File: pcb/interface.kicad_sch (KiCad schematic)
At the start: 46 parts

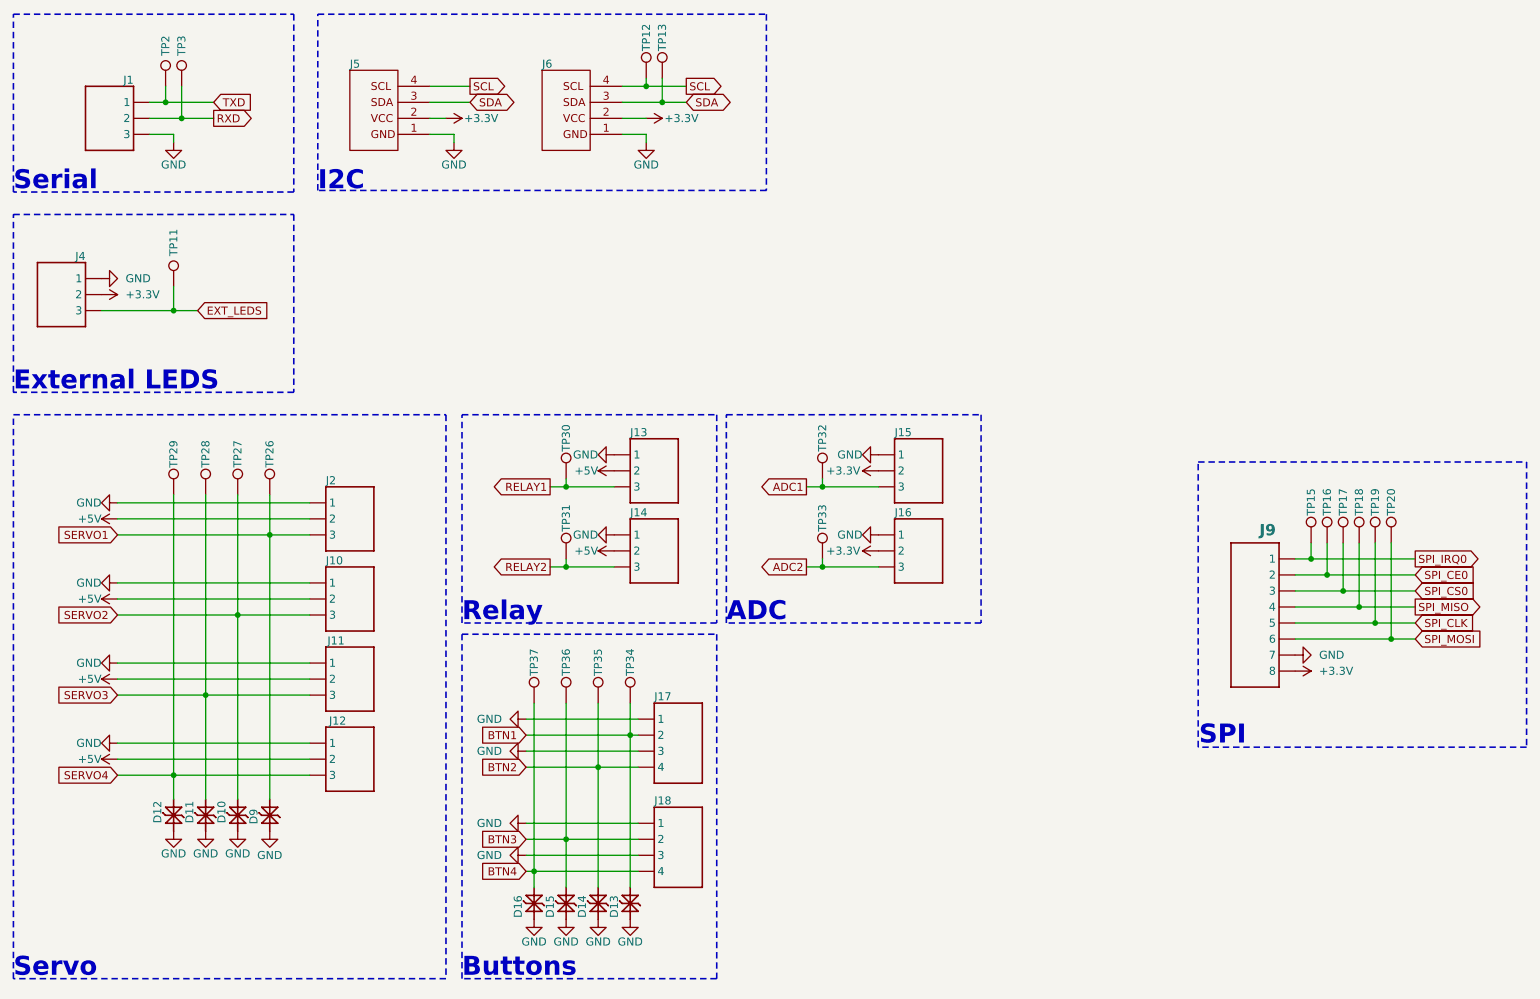
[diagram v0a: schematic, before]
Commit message: Added RF connector; re-placed and re-routed
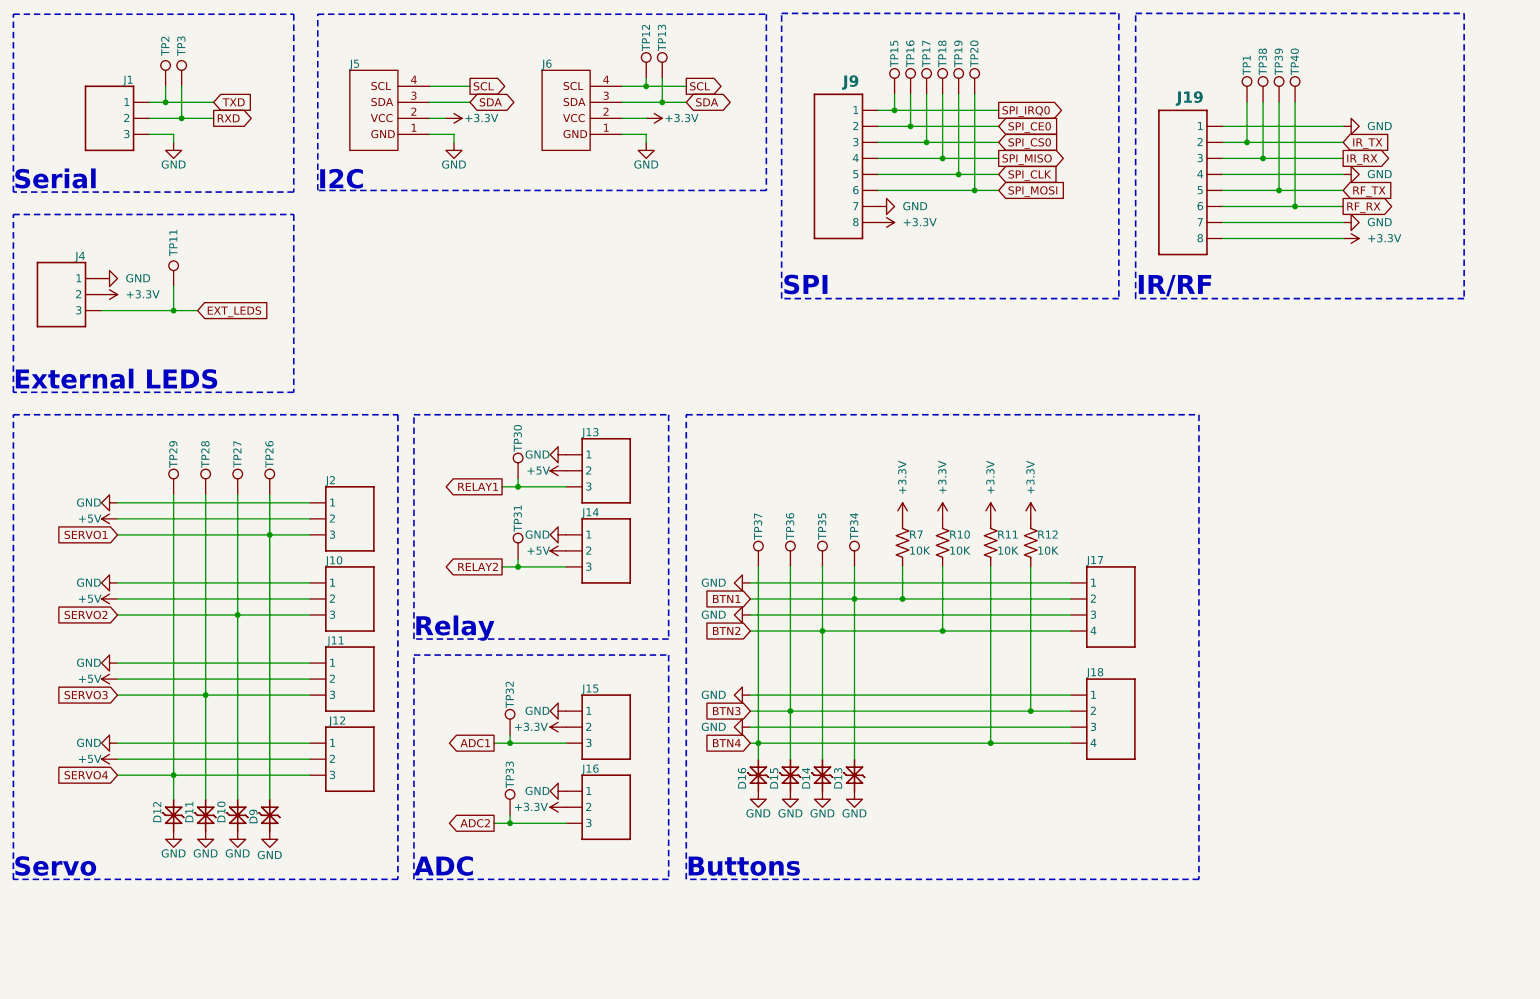
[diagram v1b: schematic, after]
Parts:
- added J19: ~, CRGM Connector:JST_SH_BM08B-SRSS-TB_1x08-1MP_P1.00mm_Vertical, symbol CRGM Connector:JST-SH-8
- added R10, R11, R12, R7: 10K, CRGM Passive:R_0603_1608Metric, symbol Device:R_US
- added TP1, TP38, TP39, TP40: ~, CRGM Mechanical:TestPoint_Pad_D1.0mm, symbol Connector:TestPoint
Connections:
- net +3.3V: now also J19.8, R10.1, R11.1, R12.1, R7.1
- net BTN1: now also R7.2
- net BTN2: now also R10.2
- net BTN3: now also R12.2
- net BTN4: now also R11.2
- net GND: now also J19.1, J19.4, J19.7
- new net IR_RX: J19.3, TP38.1
- new net IR_TX: J19.2, TP1.1
- new net RF_RX: J19.6, TP40.1
- new net RF_TX: J19.5, TP39.1
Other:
- note added: "IR/RF"
- title: Client -> Aquarius Client
- moved on the sheet: D13, D14, D15, D16, J13, J14, J15, J16, J17, J18, J9, TP15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

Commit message: Removed indictors sheet
Fixed attribute consistency with schematic and symbols
Moved logos to separate box
Updated DRC warnings/ignore
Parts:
- J1, J10, J11, J12, J13, J14, J15, J16, J2, J4: Digikey (none) -> 455-BM04B-SRSS-TBTR-ND
- J17, J18: LCSC C2919601 -> C2763614

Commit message: Updated part attributes for consistency
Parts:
- R10, R11, R12, R7: Tolerance (none) -> 5%
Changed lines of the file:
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@@
 			)
 		)
-		(property "Datasheet" "~"
+		(property "Datasheet" "https://bourns.com/docs/product-datasheets/cr.pdf?sfvrsn=574d41f6_14"
 			(at 176.53 99.06 0)
 			(effects
@@
 			)
 		)
+		(property "Tolerance" "5%"
+			(at 176.53 99.06 0)
+			(effects
+				(font
+					(size 1.27 1.27)
+				)
+				(hide yes)
+			)
+		)
 		(pin "2"
 		)
@@
 			)
 		)
-		(property "Datasheet" "~"
+		(property "Datasheet" "https://bourns.com/docs/product-datasheets/cr.pdf?sfvrsn=574d41f6_14"
 			(at 170.18 99.06 0)
 			(effects
@@
 			)
 		)
+		(property "Tolerance" "5%"
+			(at 170.18 99.06 0)
+			(effects
+				(font
+					(size 1.27 1.27)
+				)
+				(hide yes)
+			)
+		)
 		(pin "2"
 		)
@@
 			)
 		)
-		(property "Datasheet" ""
+		(property "Datasheet" "https://www.jst-mfg.com/product/pdf/eng/eSH.pdf"
 			(at 99.06 24.13 0)
 			(effects
@@
 			)
 		)
-		(property "Description" "I2C Qwiic Connector 1mm pitch JST"
+		(property "Description" "4 Position, 1mm pitch"
 			(at 103.378 38.1 0)
 			(effects
@@
 			)
 		)
-		(property "Datasheet" ""
+		(property "Datasheet" "https://www.jst-mfg.com/product/pdf/eng/eSH.pdf"
 			(at 68.58 24.13 0)
 			(effects
@@
 			)
 		)
-		(property "Description" "I2C Qwiic Connector 1mm pitch JST"
+		(property "Description" "4 Position, 1mm pitch"
 			(at 72.898 38.1 0)
 			(effects
@@
 			)
 		)
-		(property "Datasheet" "~"
+		(property "Datasheet" "https://bourns.com/docs/product-datasheets/cr.pdf?sfvrsn=574d41f6_14"
 			(at 156.21 99.06 0)
 			(effects
@@
 			)
 		)
+		(property "Tolerance" "5%"
+			(at 156.21 99.06 0)
+			(effects
+				(font
+					(size 1.27 1.27)
+				)
+				(hide yes)
+			)
+		)
 		(pin "2"
 		)
@@
 			)
 		)
-		(property "Datasheet" "~"
+		(property "Datasheet" "https://bourns.com/docs/product-datasheets/cr.pdf?sfvrsn=574d41f6_14"
 			(at 162.56 99.06 0)
 			(effects
@@
 			(at 162.56 99.06 0)
 			(effects
+				(font
+					(size 1.27 1.27)
+				)
+				(hide yes)
+			)
+		)
+		(property "Tolerance" "5%"
+			(at 162.56 99.06 0)
+			(effects

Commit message: fixed LCSC part numbers
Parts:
- J1, J10, J11, J12, J13, J14, J15, J16, J2, J4: Digikey 455-BM04B-SRSS-TBTR-ND -> 455-BM03B-SRSS-TBTR-ND; LCSC C2919601 -> C2904985; MPN BM04B-SRSS-TB -> BM03B-SRSS-TB; Mouser 306-BM04BSRSSTBTLFSN -> 306-BM03BSRSSTBTLFSN
- J17, J18: LCSC C2763614 -> C2904986
- J5, J6: LCSC C2919601 -> C2904986
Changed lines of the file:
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@@
 			)
 		)
-		(property "LCSC" "C2919601"
+		(property "LCSC" "C2904985"
 			(at 105.41 154.94 0)
 			(effects
@@
 			)
 		)
-		(property "MPN" "BM04B-SRSS-TB"
+		(property "MPN" "BM03B-SRSS-TB"
 			(at 105.41 152.908 0)
 			(effects
@@
 			)
 		)
-		(property "Mouser" "306-BM04BSRSSTBTLFSN"
+		(property "Mouser" "306-BM03BSRSSTBTLFSN"
 			(at 105.41 159.766 0)
 			(effects
@@
 			)
 		)
-		(property "Digikey" "455-BM04B-SRSS-TBTR-ND"
+		(property "Digikey" "455-BM03B-SRSS-TBTR-ND"
 			(at 105.41 157.226 0)
 			(effects
@@
 			)
 		)
-		(property "LCSC" "C2919601"
+		(property "LCSC" "C2904985"
 			(at 64.77 147.32 0)
 			(effects
@@
 			)
 		)
-		(property "MPN" "BM04B-SRSS-TB"
+		(property "MPN" "BM03B-SRSS-TB"
 			(at 64.77 145.288 0)
 			(effects
@@
 			)
 		)
-		(property "Mouser" "306-BM04BSRSSTBTLFSN"
+		(property "Mouser" "306-BM03BSRSSTBTLFSN"
 			(at 64.77 152.146 0)
 			(effects
@@
 			)
 		)
-		(property "Digikey" "455-BM04B-SRSS-TBTR-ND"
+		(property "Digikey" "455-BM03B-SRSS-TBTR-ND"
 			(at 64.77 149.606 0)
 			(effects
@@
 			)
 		)
-		(property "LCSC" "C2919601"
+		(property "LCSC" "C2904985"
 			(at 64.77 134.62 0)
 			(effects
@@
 			)
 		)
-		(property "MPN" "BM04B-SRSS-TB"
+		(property "MPN" "BM03B-SRSS-TB"
 			(at 64.77 132.588 0)
 			(effects
@@
 			)
 		)
-		(property "Mouser" "306-BM04BSRSSTBTLFSN"
+		(property "Mouser" "306-BM03BSRSSTBTLFSN"
 			(at 64.77 139.446 0)
 			(effects
@@
 			)
 		)
-		(property "Digikey" "455-BM04B-SRSS-TBTR-ND"
+		(property "Digikey" "455-BM03B-SRSS-TBTR-ND"
 			(at 64.77 136.906 0)
 			(effects
@@
 			)
 		)
-		(property "LCSC" "C2919601"
+		(property "LCSC" "C2904985"
 			(at 26.67 73.66 0)
 			(effects
@@
 			)
 		)
-		(property "MPN" "BM04B-SRSS-TB"
+		(property "MPN" "BM03B-SRSS-TB"
 			(at 26.67 71.628 0)
 			(effects
@@
 			)
 		)
-		(property "Mouser" "306-BM04BSRSSTBTLFSN"
+		(property "Mouser" "306-BM03BSRSSTBTLFSN"
 			(at 26.67 78.486 0)
 			(effects
@@
 			)
 		)
-		(property "Digikey" "455-BM04B-SRSS-TBTR-ND"
+		(property "Digikey" "455-BM03B-SRSS-TBTR-ND"
 			(at 26.67 75.946 0)
 			(effects
@@
 			)
 		)
-		(property "LCSC" "C2919601"
+		(property "LCSC" "C2904985"
 			(at 64.77 109.22 0)
 			(effects
@@
 			)
 		)
-		(property "MPN" "BM04B-SRSS-TB"
+		(property "MPN" "BM03B-SRSS-TB"
 			(at 64.77 107.188 0)
 			(effects
@@
 			)
 		)
-		(property "Mouser" "306-BM04BSRSSTBTLFSN"
+		(property "Mouser" "306-BM03BSRSSTBTLFSN"
 			(at 64.77 114.046 0)
 			(effects
@@
 			)
 		)
-		(property "Digikey" "455-BM04B-SRSS-TBTR-ND"
+		(property "Digikey" "455-BM03B-SRSS-TBTR-ND"
 			(at 64.77 111.506 0)
 			(effects
@@
 			)
 		)
-		(property "LCSC" "C2919601"
+		(property "LCSC" "C2904985"
 			(at 64.77 121.92 0)
 			(effects
@@
 			)
 		)
-		(property "MPN" "BM04B-SRSS-TB"
+		(property "MPN" "BM03B-SRSS-TB"
 			(at 64.77 119.888 0)
 			(effects
@@
 			)
 		)
-		(property "Mouser" "306-BM04BSRSSTBTLFSN"
+		(property "Mouser" "306-BM03BSRSSTBTLFSN"
 			(at 64.77 126.746 0)
 			(effects
@@
 			)
 		)
-		(property "Digikey" "455-BM04B-SRSS-TBTR-ND"
+		(property "Digikey" "455-BM03B-SRSS-TBTR-ND"
 			(at 64.77 124.206 0)
 			(effects
@@
 			)
 		)
-		(property "LCSC" "C2919601"
+		(property "LCSC" "C2904985"
 			(at 105.41 142.24 0)
 			(effects
@@
 			)
 		)
-		(property "MPN" "BM04B-SRSS-TB"
+		(property "MPN" "BM03B-SRSS-TB"
 			(at 105.41 140.208 0)
 			(effects
@@
 			)
 		)
-		(property "Mouser" "306-BM04BSRSSTBTLFSN"
+		(property "Mouser" "306-BM03BSRSSTBTLFSN"
 			(at 105.41 147.066 0)
 			(effects
@@
 			)
 		)
-		(property "Digikey" "455-BM04B-SRSS-TBTR-ND"
+		(property "Digikey" "455-BM03B-SRSS-TBTR-ND"
 			(at 105.41 144.526 0)
 			(effects
@@
 			)
 		)
-		(property "LCSC" "C2919601"
+		(property "LCSC" "C2904986"
 			(at 103.886 50.292 0)
 			(effects
@@
 			)
 		)
-		(property "LCSC" "C2919601"
+		(property "LCSC" "C2904986"
 			(at 73.406 50.292 0)
 			(effects
@@
 			)
 		)
-		(property "LCSC" "C2919601"
+		(property "LCSC" "C2904985"
 			(at 34.29 45.72 0)
 			(effects
@@
 			)
 		)
-		(property "MPN" "BM04B-SRSS-TB"
+		(property "MPN" "BM03B-SRSS-TB"
 			(at 34.29 43.688 0)
 			(effects
@@
 			)
 		)
-		(property "Mouser" "306-BM04BSRSSTBTLFSN"
+		(property "Mouser" "306-BM03BSRSSTBTLFSN"
 			(at 34.29 50.546 0)
 			(effects
@@
 			)
 		)
-		(property "Digikey" "455-BM04B-SRSS-TBTR-ND"
+		(property "Digikey" "455-BM03B-SRSS-TBTR-ND"
 			(at 34.29 48.006 0)
 			(effects
@@
 			)
 		)
-		(property "LCSC" "C2763614"
+		(property "LCSC" "C2904986"
 			(at 188.468 105.41 0)
 			(effects
@@
 			)
 		)
-		(property "LCSC" "C2919601"
+		(property "LCSC" "C2904985"
 			(at 105.41 114.3 0)
 			(effects
@@
 			)
 		)
-		(property "MPN" "BM04B-SRSS-TB"
+		(property "MPN" "BM03B-SRSS-TB"
 			(at 105.41 112.268 0)
 			(effects
@@
 			)
 		)
-		(property "Mouser" "306-BM04BSRSSTBTLFSN"
+		(property "Mouser" "306-BM03BSRSSTBTLFSN"
 			(at 105.41 119.126 0)
 			(effects
@@
 			)
 		)
-		(property "Digikey" "455-BM04B-SRSS-TBTR-ND"
+		(property "Digikey" "455-BM03B-SRSS-TBTR-ND"
 			(at 105.41 116.586 0)
 			(effects
@@
 			)
 		)
-		(property "LCSC" "C2919601"
+		(property "LCSC" "C2904985"
 			(at 105.41 101.6 0)
 			(effects
@@
 			)
 		)
-		(property "MPN" "BM04B-SRSS-TB"
+		(property "MPN" "BM03B-SRSS-TB"
 			(at 105.41 99.568 0)
 			(effects
@@
 			)
 		)
-		(property "Mouser" "306-BM04BSRSSTBTLFSN"
+		(property "Mouser" "306-BM03BSRSSTBTLFSN"
 			(at 105.41 106.426 0)
 			(effects
@@
 			)
 		)
-		(property "Digikey" "455-BM04B-SRSS-TBTR-ND"
+		(property "Digikey" "455-BM03B-SRSS-TBTR-ND"
 			(at 105.41 103.886 0)
 			(effects
@@
 			)
 		)
-		(property "LCSC" "C2763614"
+		(property "LCSC" "C2904986"
 			(at 188.468 87.63 0)
 			(effects
